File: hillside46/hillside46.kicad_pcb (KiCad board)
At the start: 2 copper layers, 142.5 x 99.9 mm, 92 parts, among them J1 Haptic, J2 TRRS, J3 Bat_Pos, J4 Bat_Neg, J5 Bat_Pos, J6 Bat_Neg, K1 SW_Key, K10 SW_Key, K11 SW_Key, K12 SW_Key, K13 SW_Key, K14 SW_Key, K15 SW_Key, K16 SW_Key, K17 SW_Key, K18 SW_Key, K19 SW_Rotary, K2 SW_Key, K20 SW_Rotary, K21 SW_Key, K22 SW_Key, K23 SW_Key, K3 SW_Key, K4 SW_Key, K5 SW_Key, K6 SW_Key, K7 SW_Key, K8 SW_Key, K9 SW_Key, SW1 SKQGAFE010, SW2 SW_Power, U1 ProMicro_r, U2 SRV05-4

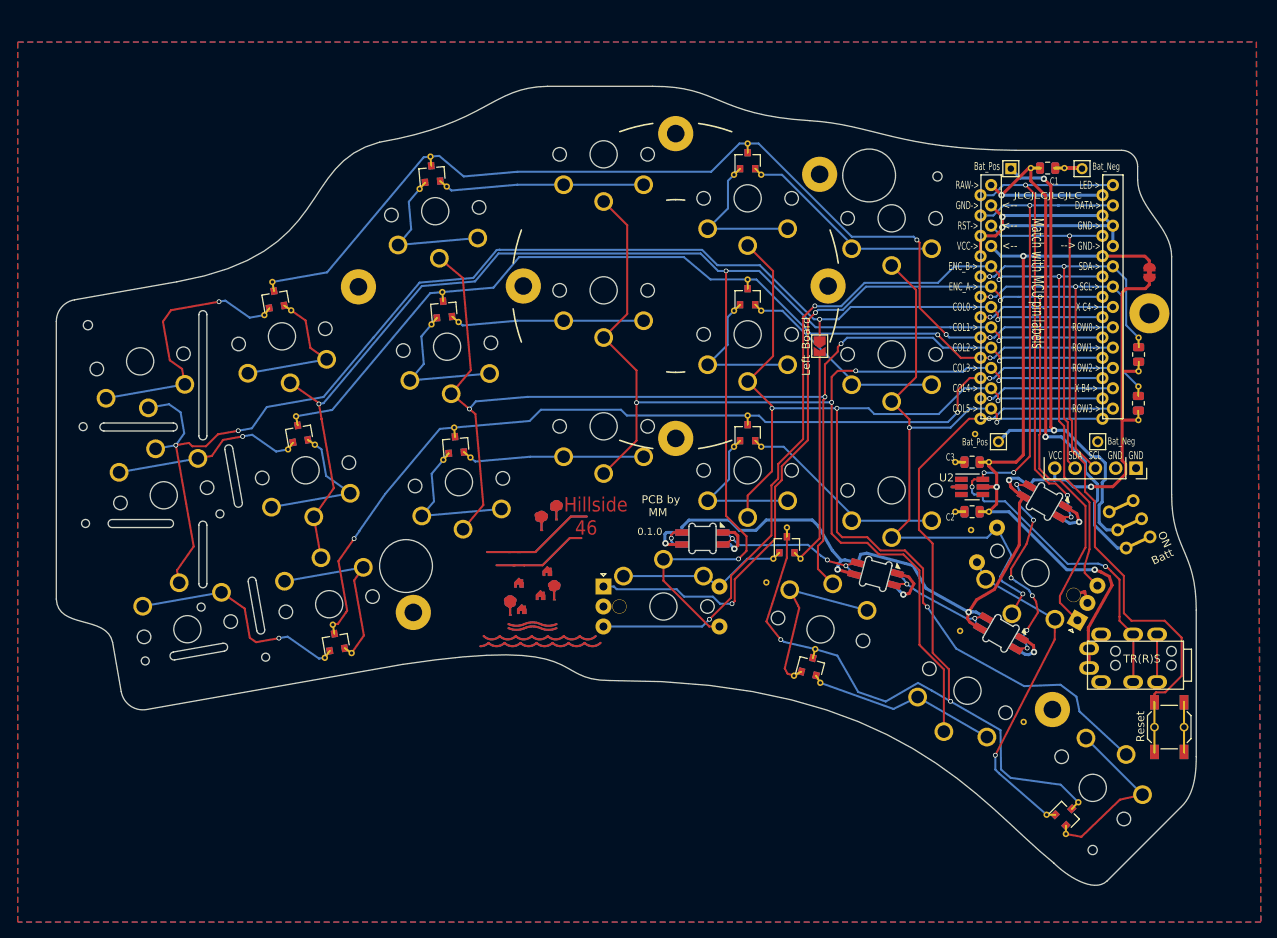
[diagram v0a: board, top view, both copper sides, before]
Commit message: Add 46 w/o 6 col
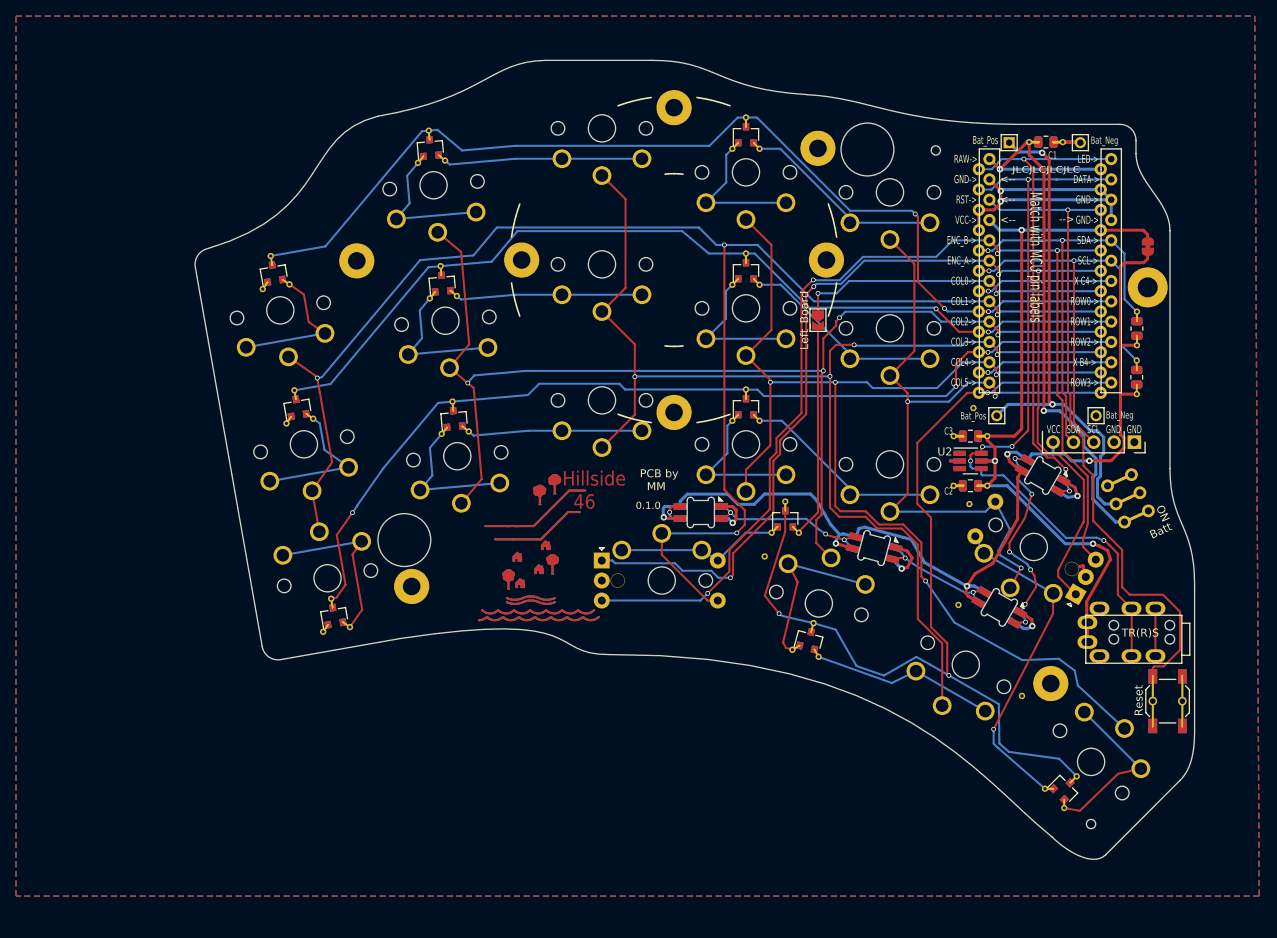
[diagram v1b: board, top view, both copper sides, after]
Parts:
- removed H10, H12, H13, H15, H2: Bumpon, hillside:Bumpon
- removed H24: ToolingHole, hillside_basic:ToolingHole_1.152mm
- removed H26, H27, H28, H29, H30, H31: Breakoff Hole, hillside_basic:HoleBreakoff_1mm
- removed K1, K13, K7: SW_Key, hillside:pg1350-R_hotswap
- moved K17 3.25 mm to (160.3, 85.4)
- moved D4 3.25 mm to (154.6, 94.0)
- moved K11 3.25 mm to (160.3, 68.4)
- moved K15 3.25 mm to (124.2, 86.9)
- moved D8 3.25 mm to (120.8, 48.4)
- moved H4 3.25 mm to (111.6, 62.5)
- moved H21 3.25 mm to (199.1, 52.6)
- moved K6 3.25 mm to (178.3, 53.9)
- moved H25 3.25 mm to (203.4, 132.9)
- moved D2 3.25 mm to (192.0, 105.8)
- moved D21 3.25 mm to (200.1, 128.5)
- moved K16 3.25 mm to (142.3, 79.9)
- moved H22 3.25 mm to (199.0, 78.1)
- moved R1 3.25 mm to (209.1, 77.1)
- moved V3 3.25 mm to (186.8, 105.5)
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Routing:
- net col0: track 164.1 -> 39.9 mm, vias 4 -> 2
- net Net-(D7-Pad1): track 23.0 -> 0.00 mm, vias 1 -> 0
- net Net-(D13-Pad1): track 17.7 -> 0.00 mm, vias 1 -> 0
- net Net-(D10-Pad1): track 13.1 -> 0.00 mm, vias 1 -> 0
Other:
- board size 142.5 x 99.9 mm -> 124.9 x 99.9 mm
- board text removed: "-2-"
- board text removed: "-br-"
- board text removed: "-cut 1-"
- board text removed: "-cut 2-"
- board text removed: "-cut 3-"
- board text removed: "-cut A-"
- board text removed: "-cut Z-"
- board text removed: "CUT"
- board text removed: "cut Y-"
